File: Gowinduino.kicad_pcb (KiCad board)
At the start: 2 copper layers, 68.6 x 53.3 mm, 63 parts, among them J1 Power, J2 Analog, J3 Digital, J4 Digital, J5 SPI, J6 JTAG, J7 USB, J8 12V, SW1 Mode, SW2 Reset, U1 GW1NSR-4CQN48P, U2 W25Q32JVSS, U3 TXB0104PW, U4 MP2122, U5 FT2232HL, U6 93LC56B, U7 XC6206-3.3, U8 L7805, Y1 12M

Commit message: Various touchups around the PCB.
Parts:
- added C22: 10µ, Capacitor_SMD:C_0805_2012Metric_Pad1.18x1.45mm_HandSolder, F.Cu at (138.3, 114.3)
- added C23: 100n, Capacitor_SMD:C_0603_1608Metric_Pad1.08x0.95mm_HandSolder, F.Cu at (143.4, 99.7)
- added L3: 3.3µ, Inductor_SMD:L_0806_2014Metric_Pad1.15x1.60mm_HandSolder, F.Cu at (135.8, 114.3)
- added R13: 36k, Resistor_SMD:R_0603_1608Metric_Pad0.98x0.95mm_HandSolder, F.Cu at (137.0, 111.1)
- added R14: 16k, Resistor_SMD:R_0603_1608Metric_Pad0.98x0.95mm_HandSolder, F.Cu at (132.6, 111.1)
- added R15: 220, Resistor_SMD:R_0603_1608Metric_Pad0.98x0.95mm_HandSolder, F.Cu at (138.3, 95.9)
- added R16: 220, Resistor_SMD:R_0603_1608Metric_Pad0.98x0.95mm_HandSolder, F.Cu at (140.8, 92.1)
- added R17: 10k, Resistor_SMD:R_0603_1608Metric_Pad0.98x0.95mm_HandSolder, F.Cu at (159.3, 87.6)
- added U10: SN74AVC4T245PW, Package_SO:TSSOP-16_4.4x5mm_P0.65mm, F.Cu at (145.9, 94.6)
- added U9: FP6161, Package_TO_SOT_SMD:SOT-23-5, F.Cu at (132.6, 114.3)
- added X1: XO32, Oscillator:Oscillator_SMD_EuroQuartz_XO32-4Pin_3.2x2.5mm, F.Cu at (140.8, 99.7)
- L1, L2: value 2.2µH -> 2.2µ; footprint Inductor_SMD:L_0805_2012Metric_Pad1.15x1.40mm_HandSolder -> Inductor_SMD:L_0806_2014Metric_Pad1.15x1.60mm_HandSolder
- moved R5 4.49 mm to (161.2, 113.7), turned to 180 degrees
- moved U3 1.27 mm to (145.9, 88.9)
- moved C17 0.63 mm to (138.3, 94.0)
- moved R11 0.63 mm to (138.3, 92.1)
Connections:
- U1 pad 18: (no net) -> /LTX
- U1 pad 19: (no net) -> /LRX
- U1 pad 20: (no net) -> /MCLK
- U5 pad 38: (no net) -> /RX
- U5 pad 39: (no net) -> /TX
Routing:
- net /RX: track 0.00 -> 23.4 mm, vias 0 -> 2
- net /TX: track 0.00 -> 17.9 mm, vias 0 -> 2
- net +3V3: track 155.3 -> 168.7 mm, vias 13 -> 15
- net +1V8: track 43.3 -> 50.6 mm, vias 3 -> 4
- net /CLK: track 0.00 -> 6.04 mm
- net Net-(R13-Pad2): track 0.00 -> 5.47 mm
- net +5V: track 114.3 -> 119.6 mm
- net /LTX: track 0.00 -> 5.14 mm
- net /LRX: track 0.00 -> 4.71 mm
- net Net-(R15-Pad2): track 0.00 -> 4.51 mm
- net /MCLK: track 0.00 -> 4.27 mm
- net /TCK: track 28.3 -> 32.3 mm
- net Net-(R16-Pad2): track 0.00 -> 2.49 mm
- net Net-(L3-Pad2): track 0.00 -> 2.26 mm
- net /13: track 17.6 -> 15.5 mm
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
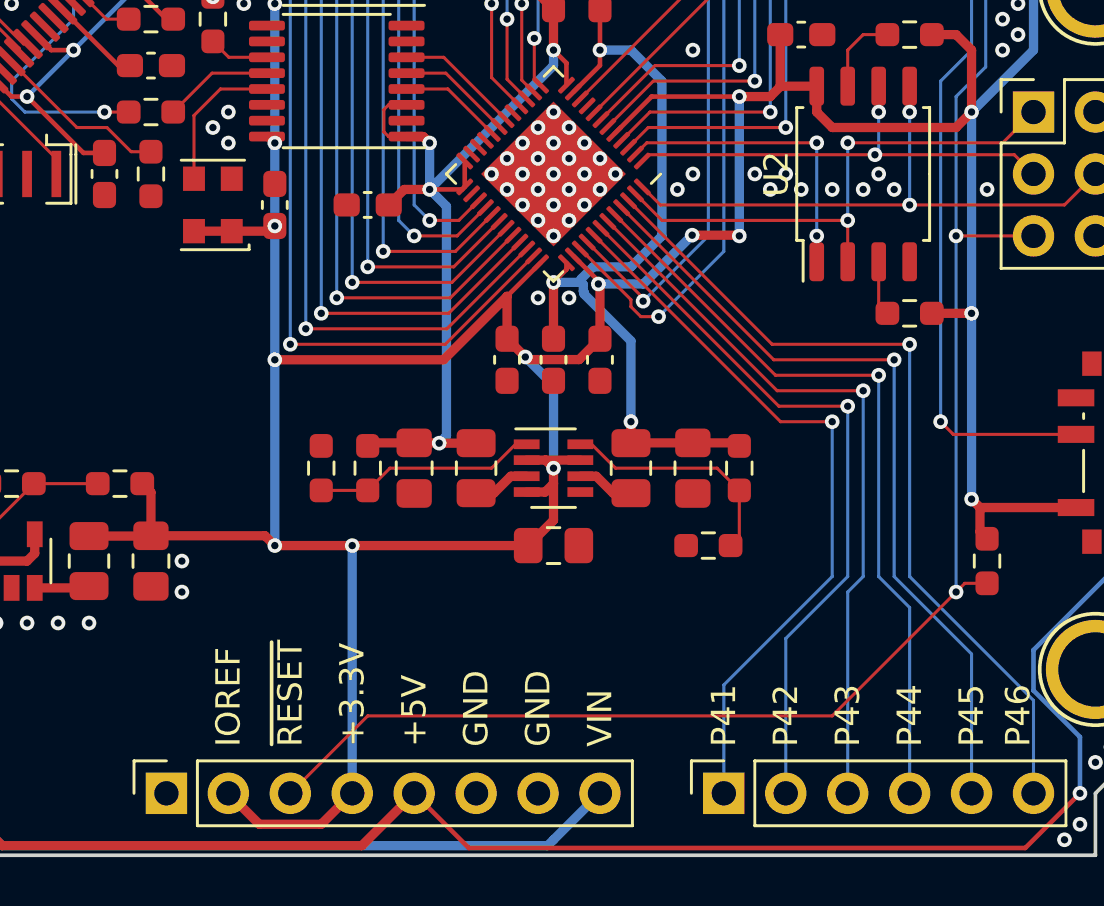
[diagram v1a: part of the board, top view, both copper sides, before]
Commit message: Schematics: LEDs
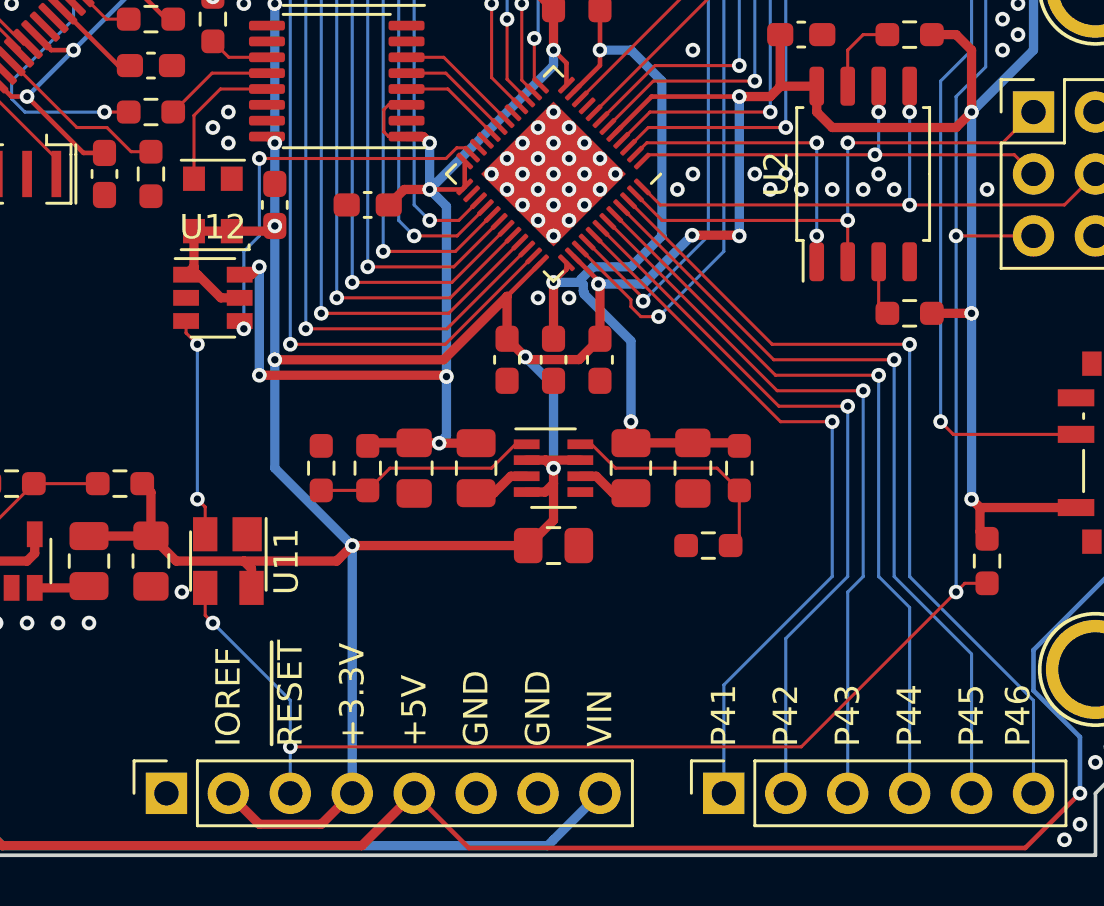
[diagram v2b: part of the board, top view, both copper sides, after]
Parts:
- added U11: MAX811SEUS-T, Package_TO_SOT_SMD:SOT-143, F.Cu at (141.5, 114.3)
- added U12: SN74LVC1T45DBV, Package_TO_SOT_SMD:SOT-23-6, F.Cu at (140.8, 103.5)
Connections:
- U1 pad 23: (no net) -> /~RST
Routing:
- net /~RST: track 0.00 -> 16.6 mm, vias 0 -> 2
- net +1V8: track 50.6 -> 63.7 mm, vias 4 -> 7
- net /~RESET: track 131.1 -> 140.2 mm, vias 4 -> 6
- net Net-(U11-Pad2): track 0.00 -> 9.07 mm, vias 0 -> 2
- net +3V3: track 168.7 -> 176.3 mm, vias 15 -> 14
- net GND: vias 202 -> 201

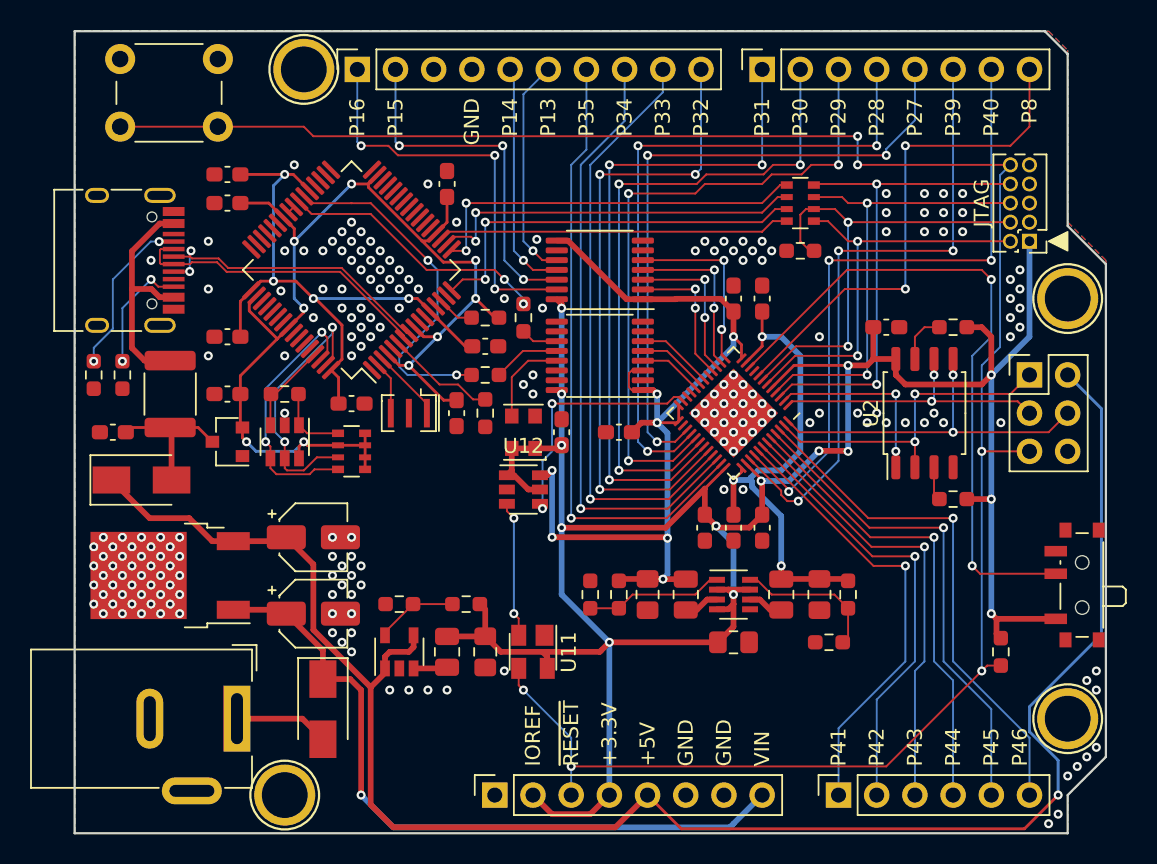
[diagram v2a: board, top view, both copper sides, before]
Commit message: PCB: Layout done, now stitching vias
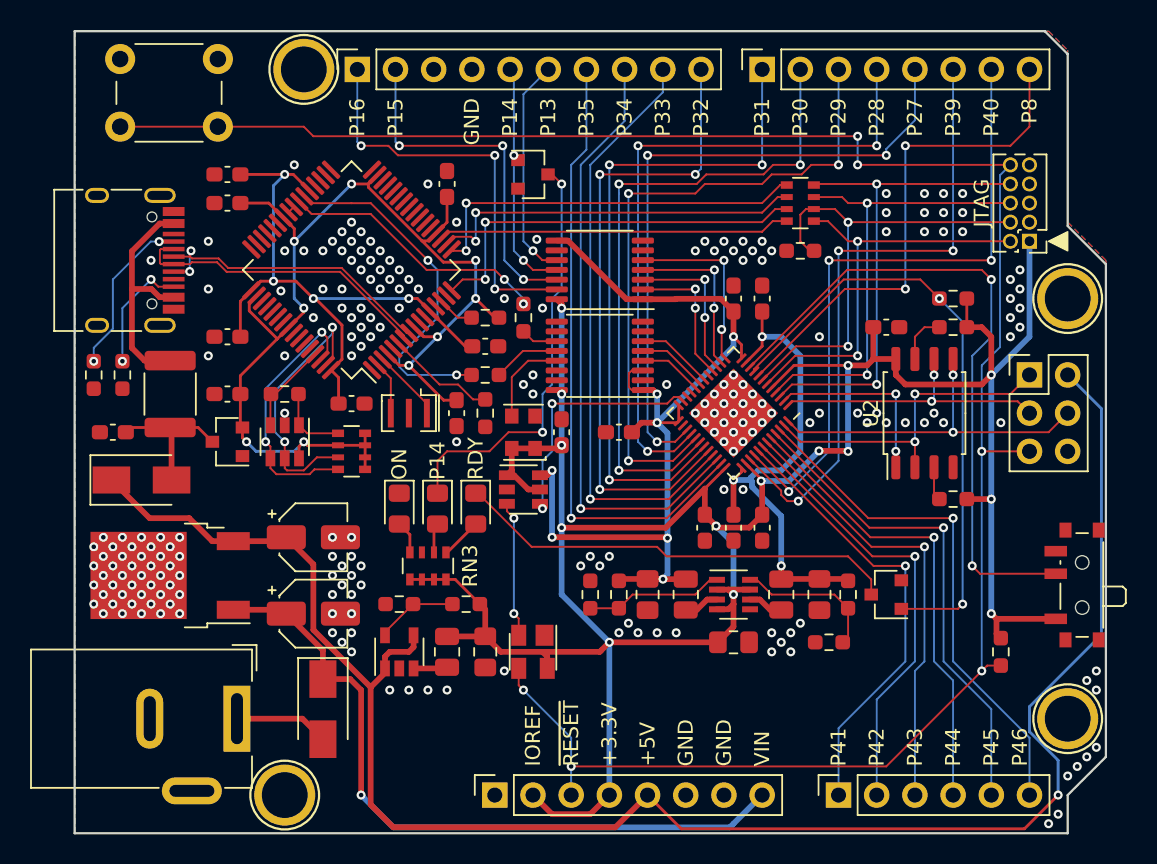
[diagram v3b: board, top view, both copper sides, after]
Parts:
- added D3: Done, LED_SMD:LED_0805_2012Metric_Pad1.15x1.40mm_HandSolder, F.Cu at (137.7, 104.8)
- added D4: L, LED_SMD:LED_0805_2012Metric_Pad1.15x1.40mm_HandSolder, F.Cu at (135.1, 104.8)
- added D5: Power, LED_SMD:LED_0805_2012Metric_Pad1.15x1.40mm_HandSolder, F.Cu at (132.6, 104.8)
- added Q1: 2N7002, Package_TO_SOT_SMD:SOT-23, F.Cu at (165.0, 110.5)
- added Q2: 2N7002, Package_TO_SOT_SMD:SOT-23, F.Cu at (141.5, 82.5)
- added R18: 4.7k, Resistor_SMD:R_0603_1608Metric_Pad0.98x0.95mm_HandSolder, F.Cu at (169.4, 90.8)
- added RN3: 220, Resistor_SMD:R_Array_Convex_4x0603, F.Cu at (134.5, 108.6)
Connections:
- U1 pad 9: (no net) -> /DONE
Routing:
- net /DONE: track 0.00 -> 40.6 mm, vias 0 -> 2
- net Net-(D3-Pad1): track 0.00 -> 29.7 mm
- net Net-(D4-Pad1): track 0.00 -> 28.1 mm, vias 0 -> 2
- net +3V3: track 176.3 -> 183.5 mm
- net Net-(D3-Pad2): track 0.00 -> 2.76 mm
- net Net-(D5-Pad2): track 0.00 -> 2.18 mm
- net Net-(D4-Pad2): track 0.00 -> 1.98 mm
- net /13: track 15.5 -> 16.0 mm, vias 1 -> 2
- net GND: vias 201 -> 218
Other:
- board text added: "ON"
- board text added: "RDY"

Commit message: FInals: front-side silkscreens
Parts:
- added R19: 1k, Resistor_SMD:R_0603_1608Metric_Pad0.98x0.95mm_HandSolder, F.Cu at (165.6, 104.1)
- R17: value 10k -> 4.7k
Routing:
- net /SCLK: track 19.4 -> 26.8 mm, vias 2 -> 3
- net GND: vias 218 -> 405
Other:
- board text added: "AUTOBOOT SPI BOOT"
- board text added: "Gowinduino"
- board text added: "SushiBits M1DKv1-GW1MCU"
- board text added: "© 2021 Max Chan. https://sushibits.info/"

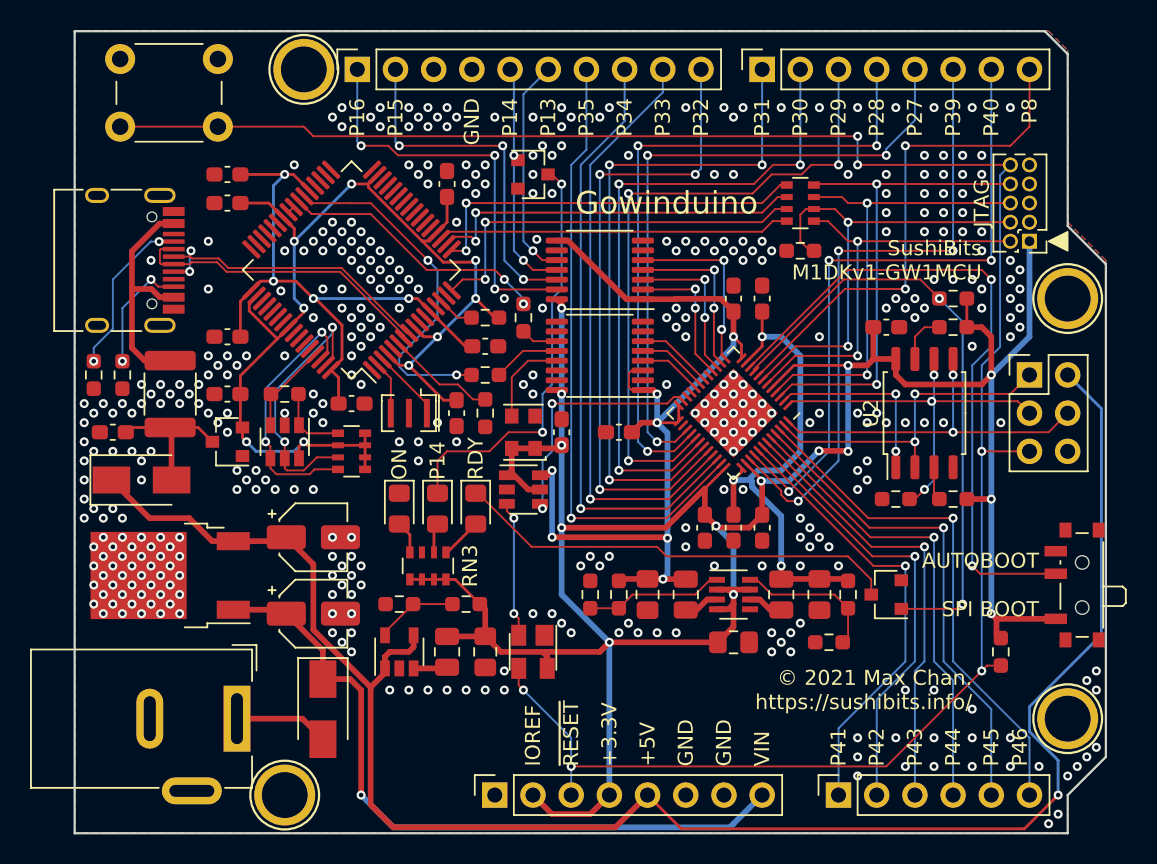
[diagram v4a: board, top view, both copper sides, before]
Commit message: Name on the drawings
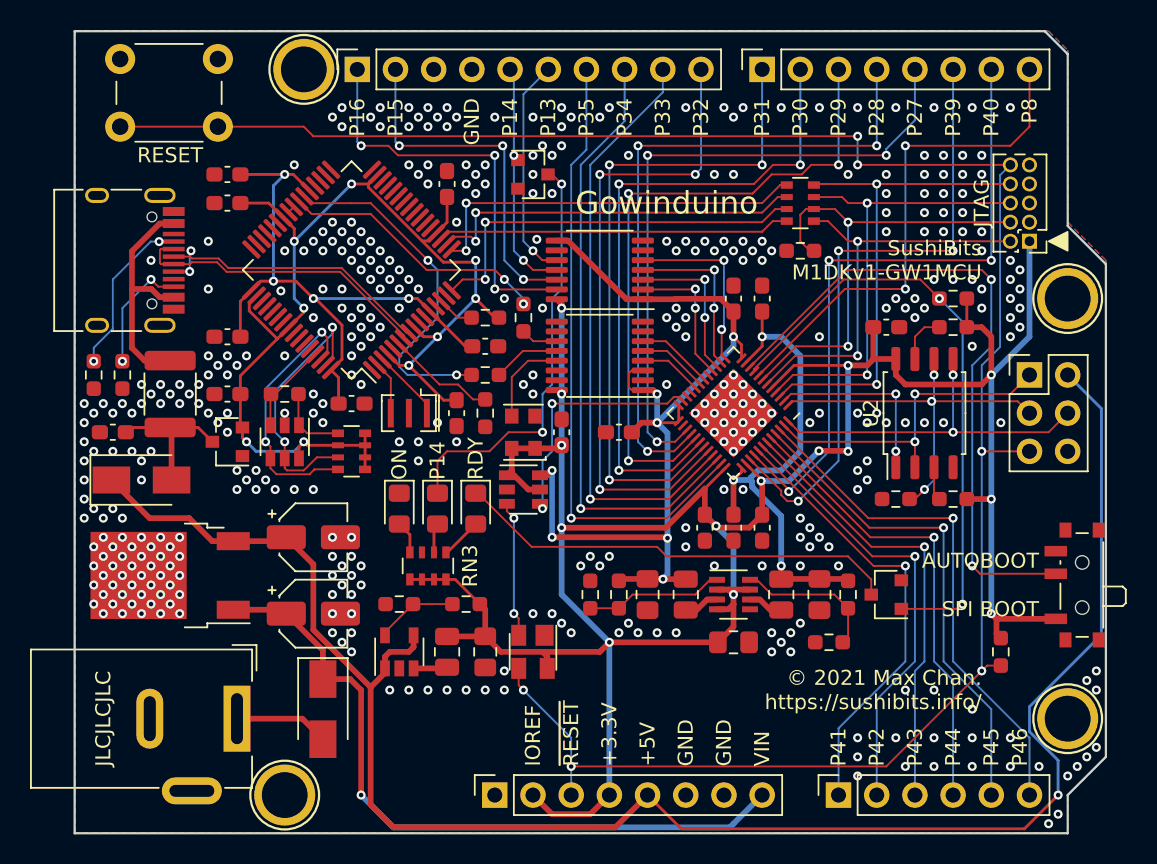
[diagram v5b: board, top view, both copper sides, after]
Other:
- board text added: "JLCJLCJLC"
- board text added: "RESET"
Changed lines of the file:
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@@
   (general
     (thickness 1.6)
-    (drawings 60)
+    (drawings 62)
     (tracks 1292)
     (zones 0)
@@
     (pad 1 thru_hole circle (at 0 0) (size 4.064 4.064) (drill 3.048) (layers *.Cu *.Mask F.SilkS))
   )
+  (gr_text RESET (at 117.348 81.28) (layer F.SilkS)
+    (effects (font (size 1 1) (thickness 0.15)))
+  )
+  (gr_text JLCJLCJLC (at 112.903 118.745 90) (layer F.SilkS)
+    (effects (font (size 1 1) (thickness 0.15)))
+  )
   (gr_text "SushiBits\nM1DKv1-GW1MCU" (at 171.323 88.265) (layer F.SilkS)
     (effects (font (size 1 1) (thickness 0.15)) (justify right))
   )
-  (gr_text "© 2021 Max Chan.\nhttps://sushibits.info/" (at 170.688 116.84) (layer F.SilkS)
+  (gr_text "© 2021 Max Chan.\nhttps://sushibits.info/" (at 171.323 116.84) (layer F.SilkS)
     (effects (font (size 1 1) (thickness 0.15)) (justify right))
   )

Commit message: OSHW and ESD symbols
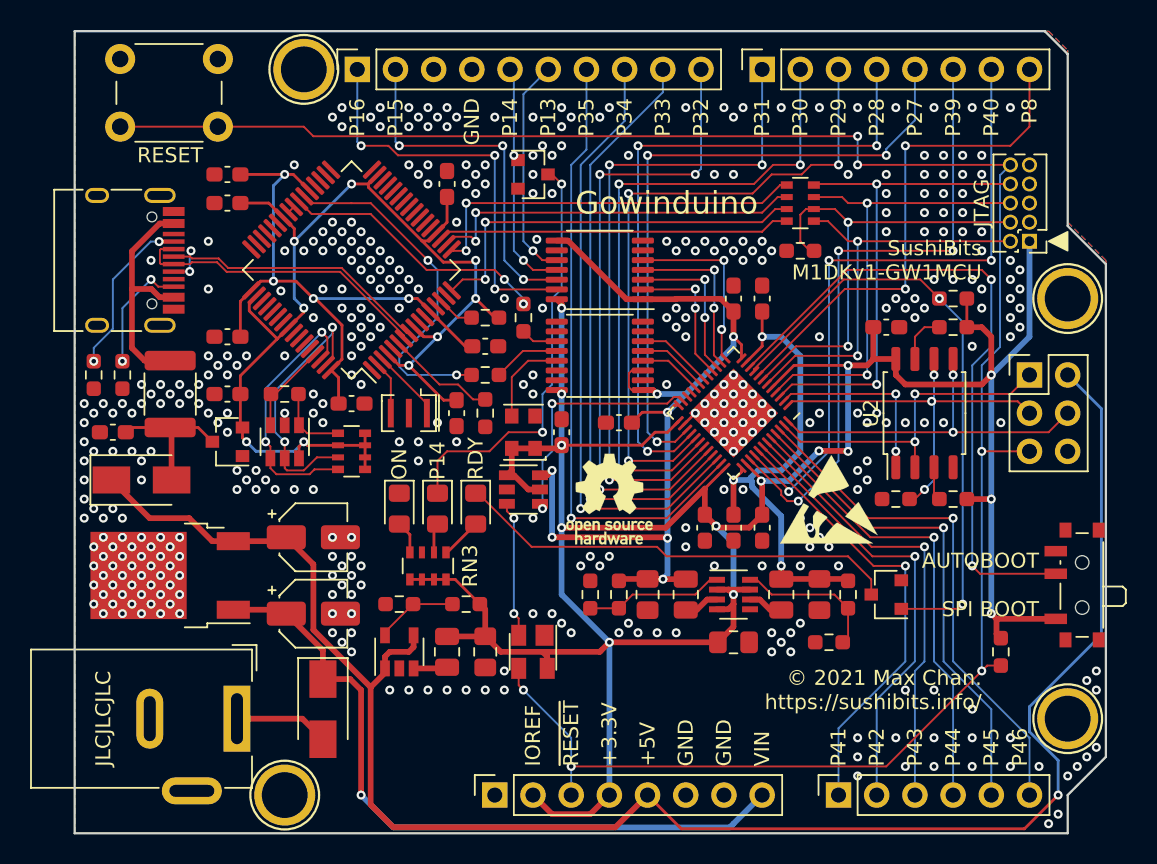
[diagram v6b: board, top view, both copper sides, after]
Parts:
- added REF**: ESD-Logo_6.6x6mm_SilkScreen, Symbol:ESD-Logo_6.6x6mm_SilkScreen, F.Cu at (161.2, 104.1)
- added REF**: OSHW-Logo_5.7x6mm_SilkScreen, Symbol:OSHW-Logo_5.7x6mm_SilkScreen, F.Cu at (146.6, 104.1)
- moved C5 0.63 mm to (147.2, 99.1)
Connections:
- U1 pad 25: +1V8 -> +3V3
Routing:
- net +3V3: track 183.5 -> 192.1 mm
- net GND: track 0.00 -> 3.70 mm, vias 405 -> 406
- net +1V8: track 63.7 -> 62.2 mm
